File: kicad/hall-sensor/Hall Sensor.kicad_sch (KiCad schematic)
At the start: 5 parts, among them J8701 ZX-SH1_0-4PLT, U8701 CC6201ST

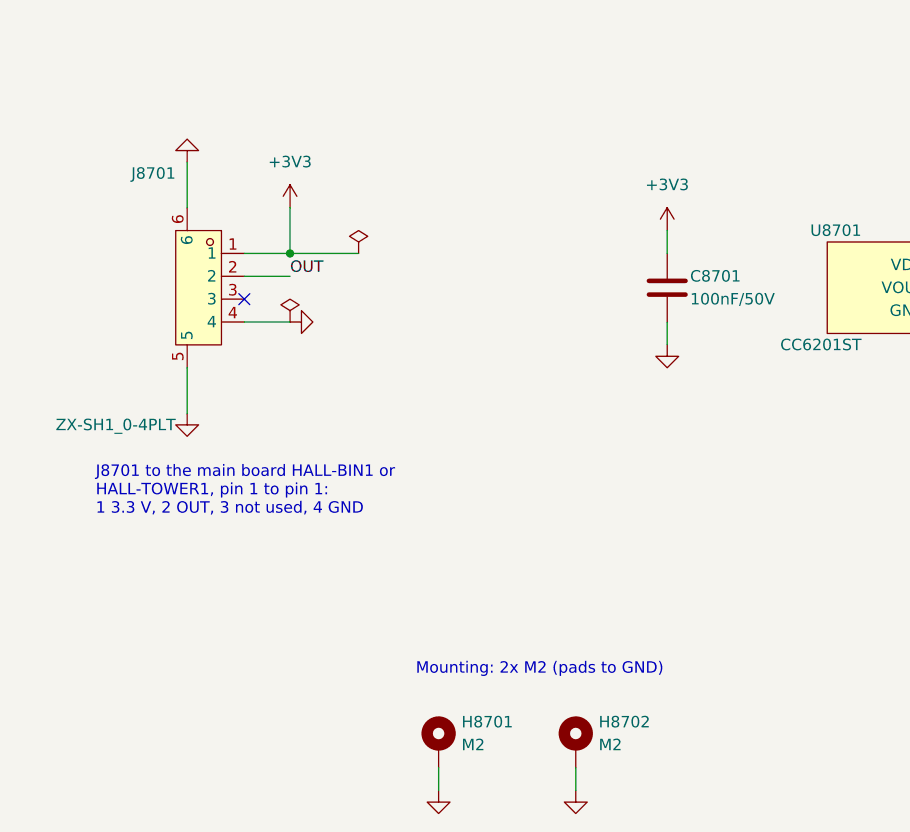
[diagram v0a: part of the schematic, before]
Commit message: LiDAR header, shunt, holes, Hall connector, INT pullup fix
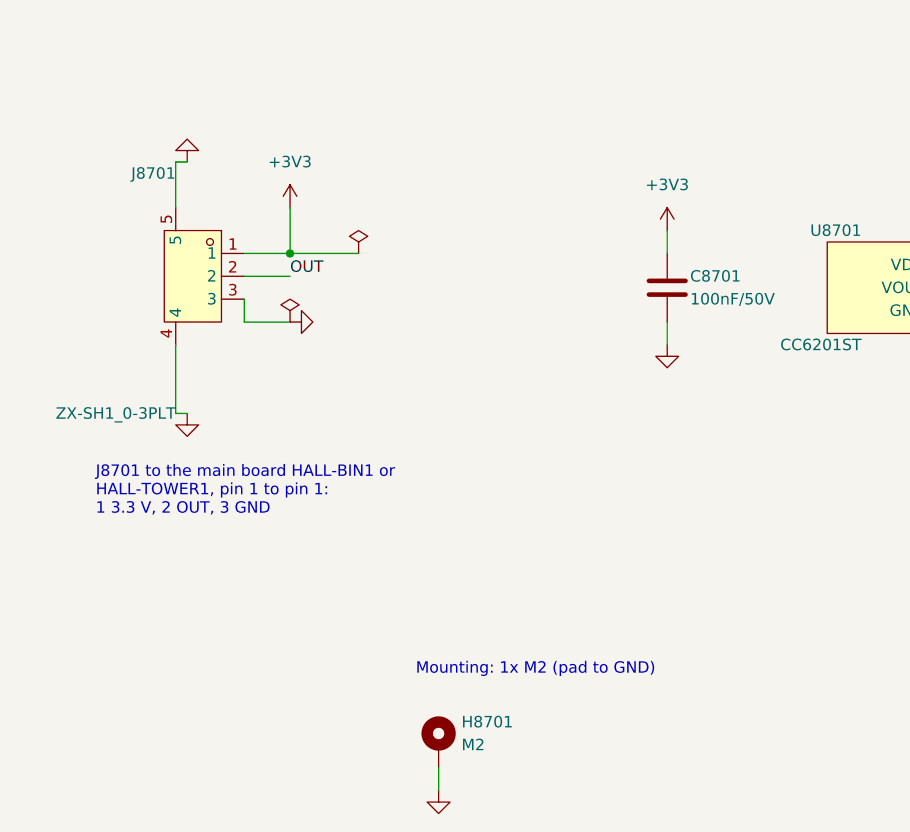
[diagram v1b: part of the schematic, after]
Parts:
- removed H8702: M2, MountingHole:MountingHole_2.2mm_M2_Pad, symbol Mechanical:MountingHole_Pad
- removed J8701: ZX-SH1_0-4PLT, JLCImport:ZX-SH1_0-4PLT, symbol JLCImport:ZX-SH1_0-4PLT
- added J8701: ZX-SH1_0-3PLT, JLCImport:ZX-SH1_0-3PLT, symbol JLCImport:ZX-SH1_0-3PLT
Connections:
- net +3V3: now also J8701.1
- net GND: now also J8701.3, J8701.4, J8701.5
- net OUT: now also J8701.2
- no-connect marks 1 -> 0
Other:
- note added: "J8701 to the main board HALL-BIN1 or HALL-TOWER1, pin 1 to pin 1: 1 3.3 V, 2 OUT, 3 GND"
- note added: "Mounting: 1x M2 (pad to GND)"
- note removed: "J8701 to the main board HALL-BIN1 or HALL-TOWER1, pin 1 to pin 1: 1 3.3 V, 2 OUT, 3 not used, 4 GND"
- note removed: "Mounting: 2x M2 (pads to GND)"
